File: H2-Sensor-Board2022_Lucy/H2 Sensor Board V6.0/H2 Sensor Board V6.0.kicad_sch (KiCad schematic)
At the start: 1 part, among them U1 STM32L442KCUx

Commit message: W
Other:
- added sheet Sheet2 (untitled.kicad_sch)
- moved on the sheet: U1
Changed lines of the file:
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@@
 (kicad_sch (version 20230121) (generator eeschema)
   (paper "A4")
-  (wire (pts (xy 109.22 100.33) (xy 113.03 100.33))
+  (wire (pts (xy 77.47 76.2) (xy 81.28 76.2))
     (stroke (width 0) (type default))
   )
-  (wire (pts (xy 109.22 95.25) (xy 119.38 95.25))
+  (wire (pts (xy 77.47 71.12) (xy 87.63 71.12))
     (stroke (width 0) (type default))
   )
-  (wire (pts (xy 109.22 102.87) (xy 120.65 102.87))
+  (wire (pts (xy 77.47 78.74) (xy 88.9 78.74))
     (stroke (width 0) (type default))
   )
-  (wire (pts (xy 71.12 67.31) (xy 83.82 67.31))
+  (wire (pts (xy 39.37 43.18) (xy 52.07 43.18))
     (stroke (width 0) (type default))
   )
-  (wire (pts (xy 109.22 97.79) (xy 119.38 97.79))
+  (wire (pts (xy 77.47 73.66) (xy 87.63 73.66))
     (stroke (width 0) (type default))
   )
-  (wire (pts (xy 71.12 72.39) (xy 83.82 72.39))
+  (wire (pts (xy 39.37 48.26) (xy 52.07 48.26))
     (stroke (width 0) (type default))
   )
-  (wire (pts (xy 109.22 67.31) (xy 123.19 67.31))
+  (wire (pts (xy 77.47 43.18) (xy 91.44 43.18))
     (stroke (width 0) (type default))
   )
-  (label "JTCK" (at 120.65 102.87 0) (fields_autoplaced)
+  (label "JTCK" (at 88.9 78.74 0) (fields_autoplaced)
     (effects (font (size 1.27 1.27)) (justify left bottom))
   )
-  (label "JTMS" (at 113.03 100.33 0) (fields_autoplaced)
+  (label "JTMS" (at 81.28 76.2 0) (fields_autoplaced)
     (effects (font (size 1.27 1.27)) (justify left bottom))
   )
-  (label "RESET" (at 71.12 66.04 0) (fields_autoplaced)
+  (label "RESET" (at 39.37 41.91 0) (fields_autoplaced)
     (effects (font (size 1.27 1.27)) (justify left bottom))
   )
-  (label "Boot0" (at 64.77 73.66 0) (fields_autoplaced)
+  (label "Boot0" (at 33.02 49.53 0) (fields_autoplaced)
     (effects (font (size 1.27 1.27)) (justify left bottom))
   )
-  (global_label "H2Sens_In" (shape input) (at 123.19 67.31 0) (fields_autoplaced)
+  (global_label "H2Sens_In" (shape input) (at 91.44 43.18 0) (fields_autoplaced)
     (effects (font (size 1.27 1.27)) (justify left))
-    (property "Intersheetrefs" "${INTERSHEET_REFS}" (at 135.9118 67.31 0)
+    (property "Intersheetrefs" "${INTERSHEET_REFS}" (at 104.1618 43.18 0)
       (effects (font (size 1.27 1.27)) (justify left) hide)
     )
   )
-  (global_label "CAN_RX" (shape input) (at 119.38 95.25 0) (fields_autoplaced)
+  (global_label "CAN_RX" (shape input) (at 87.63 71.12 0) (fields_autoplaced)
     (effects (font (size 1.27 1.27)) (justify left))
-    (property "Intersheetrefs" "${INTERSHEET_REFS}" (at 129.5014 95.25 0)
+    (property "Intersheetrefs" "${INTERSHEET_REFS}" (at 97.7514 71.12 0)
       (effects (font (size 1.27 1.27)) (justify left) hide)
     )
   )
-  (global_label "CAN_TX" (shape input) (at 119.38 97.79 0) (fields_autoplaced)
+  (global_label "CAN_TX" (shape input) (at 87.63 73.66 0) (fields_autoplaced)
     (effects (font (size 1.27 1.27)) (justify left))
-    (property "Intersheetrefs" "${INTERSHEET_REFS}" (at 129.199 97.79 0)
+    (property "Intersheetrefs" "${INTERSHEET_REFS}" (at 97.449 73.66 0)
       (effects (font (size 1.27 1.27)) (justify left) hide)
     )
   )
-  (symbol (lib_id "MCU_ST_STM32L4:STM32L442KCUx") (at 96.52 87.63 0) (unit 1)
+  (symbol (lib_id "MCU_ST_STM32L4:STM32L442KCUx") (at 64.77 63.5 0) (unit 1)
     (in_bom yes) (on_board yes) (dnp no) (fields_autoplaced)
-    (property "Reference" "U1" (at 98.4759 113.03 0)
+    (property "Reference" "U1" (at 66.7259 88.9 0)
       (effects (font (size 1.27 1.27)) (justify left))
     )
-    (property "Value" "STM32L442KCUx" (at 98.4759 115.57 0)
+    (property "Value" "STM32L442KCUx" (at 66.7259 91.44 0)
       (effects (font (size 1.27 1.27)) (justify left))
     )
-    (property "Footprint" "Package_DFN_QFN:QFN-32-1EP_5x5mm_P0.5mm_EP3.45x3.45mm" (at 86.36 110.49 0)
+    (property "Footprint" "Package_DFN_QFN:QFN-32-1EP_5x5mm_P0.5mm_EP3.45x3.45mm" (at 54.61 86.36 0)
       (effects (font (size 1.27 1.27)) (justify right) hide)
     )
-    (property "Datasheet" "https://www.st.com/resource/en/datasheet/stm32l442kc.pdf" (at 96.52 87.63 0)
+    (property "Datasheet" "https://www.st.com/resource/en/datasheet/stm32l442kc.pdf" (at 64.77 63.5 0)
       (effects (font (size 1.27 1.27)) hide)
     )
@@
       )
     )
+  )
+  (sheet (at 177.8 43.18) (size 83.82 50.8) (fields_autoplaced)
+    (stroke (width 0.1524) (type solid))
+    (fill (color 0 0 0 0.0000))
+    (property "Sheetname" "Sheet2" (at 177.8 42.4684 0)
+      (effects (font (size 1.27 1.27)) (justify left bottom))
+    )
+    (property "Sheetfile" "untitled.kicad_sch" (at 177.8 94.5646 0)
+      (effects (font (size 1.27 1.27)) (justify left top))
+    )
+    (instances
+      (project "H2 Sensor Board V6.0"
+        (path "/61fdd4a1-2d1e-44dc-8644-252e12d35745" (page "2"))
+      )
+    )

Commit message: up
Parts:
- added C10: 10n, symbol Device:C
- added C11, C12: 1u, symbol Device:C
- added C7, C8: 100n, symbol Device:C
- added C9: 10u, symbol Device:C
- added FB1: FerriteBead, symbol Device:FerriteBead
- added R1: 10k, symbol Device:R_US
- added SW1: SW_SPDT, symbol Switch:SW_SPDT
- added Y1: Crystal, symbol Device:Crystal
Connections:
- net +3.3V: now reaches U1.1 (VDD)
- net +3.3V: now also U1.17 (VDD), C7.1, C8.1, C9.1, SW1.3 (C)
- net GND: now reaches U1.16 (VSS), U1.32 (VSS), U1.33 (VSS)
- net GND: now also C10.2, C11.2, C12.2, C7.2, C8.2, C9.2, SW1.1 (A)
- net at U1.31 (PH3): now also R1.2
- net NRST: now reaches U1.4 (NRST)
- net +3.3VA: now reaches U1.5 (VDDA)
- net +3.3VA: now also C10.1, C11.1, FB1.1
- net CAN_RX: no longer names the net of U1.21 (PA11)
- net CAN_TX: no longer names the net of U1.22 (PA12)
- net H2Sens_In: no longer names the net of U1.6 (PA0)
- net JTCK: no longer names the net of U1.24 (PA14)
- net JTMS: no longer names the net of U1.23 (PA13)
- new net: C12.1, FB1.2
- new net: R1.1, SW1.2 (B)

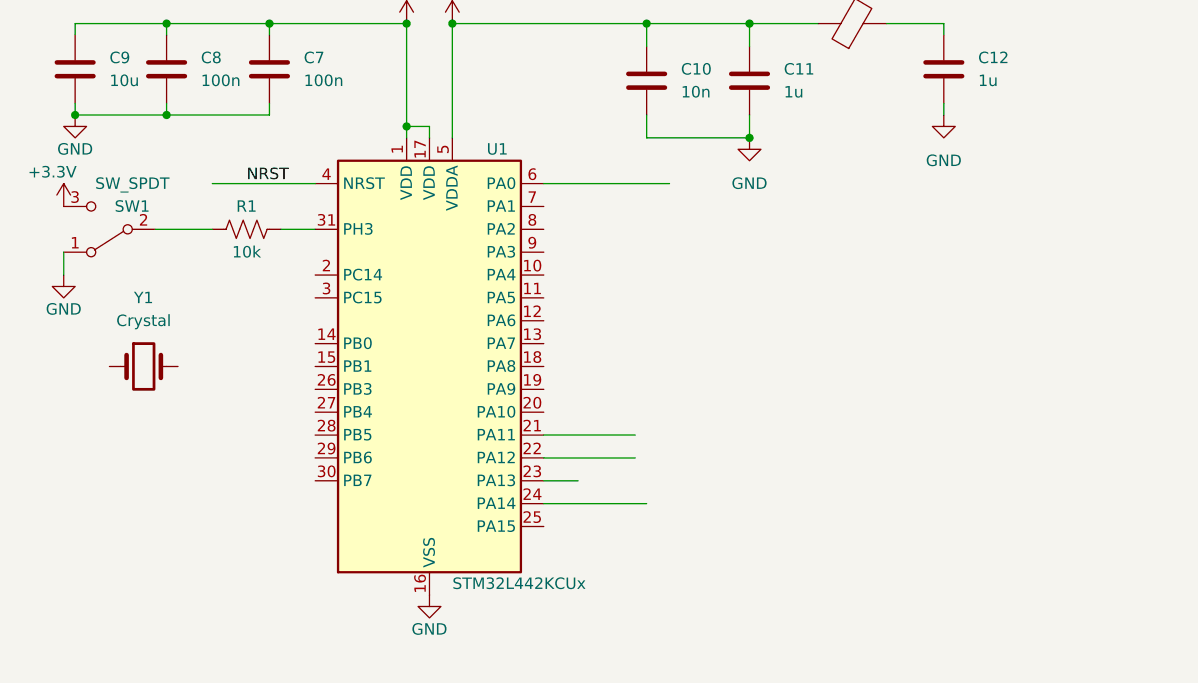
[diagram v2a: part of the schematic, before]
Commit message: MCU Pinout
First Rev of MCU Pinout/setup
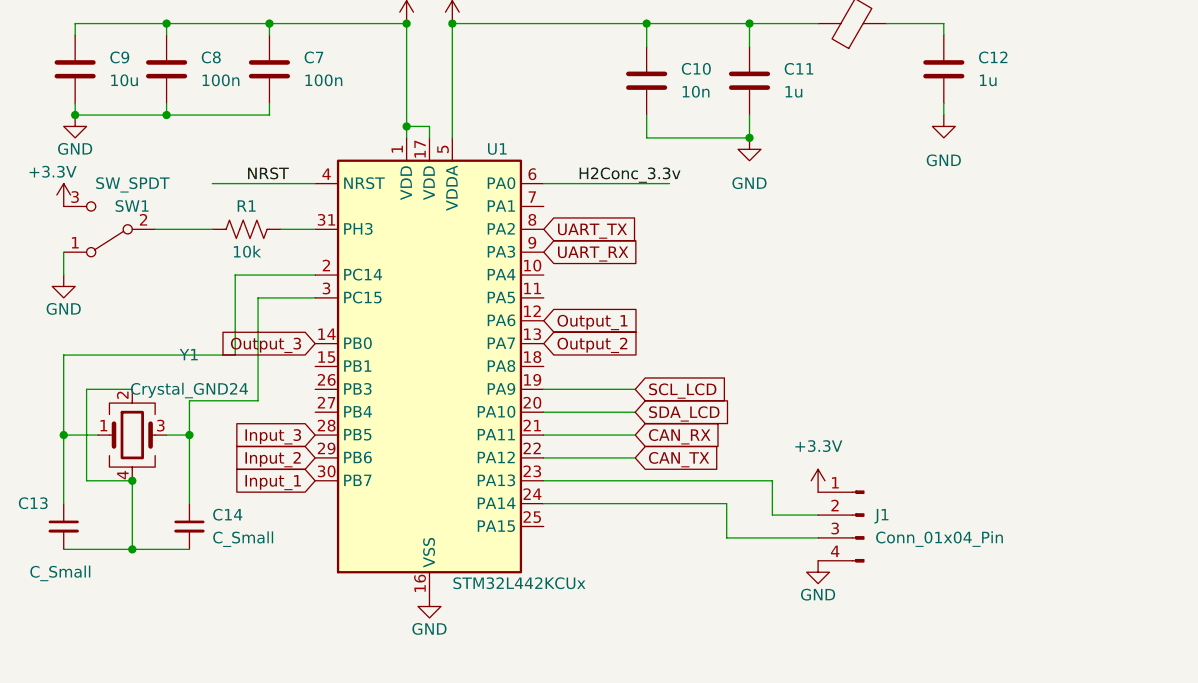
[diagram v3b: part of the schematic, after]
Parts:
- removed Y1: Crystal, symbol Device:Crystal
- added C13, C14: C_Small, symbol Device:C_Small
- added J1: Conn_01x04_Pin, symbol Connector:Conn_01x04_Pin
- added Y1: Crystal_GND24, symbol Device:Crystal_GND24
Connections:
- net +3.3V: now also J1.1 (Pin_1)
- net GND: now also J1.4 (Pin_4)
- net Output_1: now reaches U1.12 (PA6)
- net Output_2: now reaches U1.13 (PA7)
- net Output_3: now reaches U1.14 (PB0)
- net SCL_LCD: now reaches U1.19 (PA9)
- net at U1.2 (PC14): now also C13.1, Y1.1
- net SDA_LCD: now reaches U1.20 (PA10)
- net CAN_RX: now reaches U1.21 (PA11)
- net CAN_TX: now reaches U1.22 (PA12)
- net at U1.23 (PA13): now also J1.2 (Pin_2)
- net at U1.24 (PA14): now also J1.3 (Pin_3)
- net Input_3: now reaches U1.28 (PB5)
- net Input_2: now reaches U1.29 (PB6)
- net at U1.3 (PC15): now also C14.1, Y1.3
- net Input_1: now reaches U1.30 (PB7)
- net H2Conc_3.3v: now reaches U1.6 (PA0)
- net UART_TX: now reaches U1.8 (PA2)
- net UART_RX: now reaches U1.9 (PA3)
- new net: C13.2, C14.2, Y1.2, Y1.4
